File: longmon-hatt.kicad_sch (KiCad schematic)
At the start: 3 parts

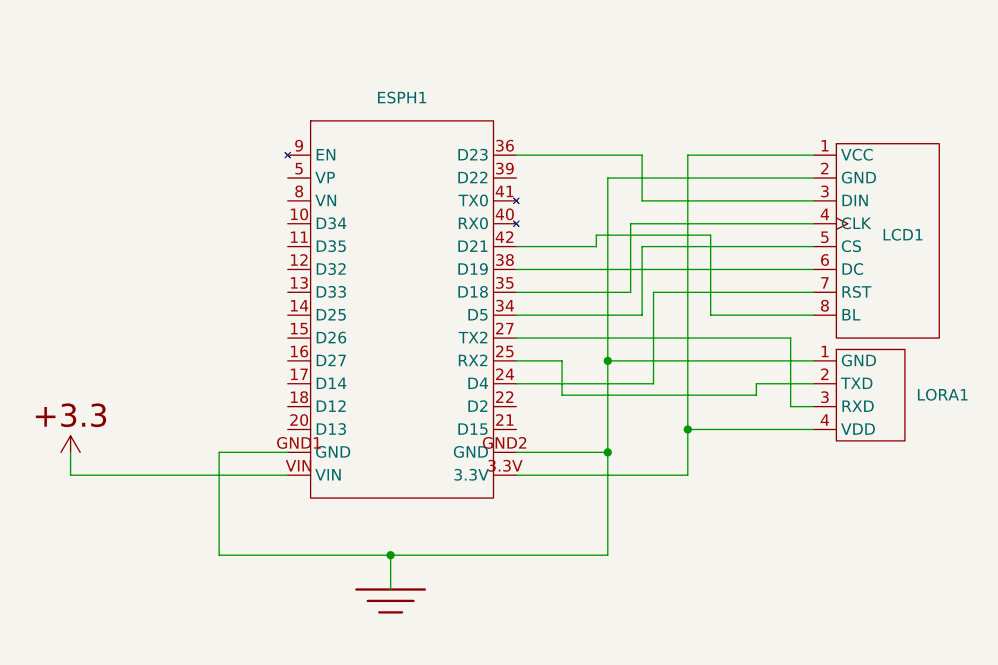
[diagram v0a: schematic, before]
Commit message: Modify LoRa module to include additional pin (unused)
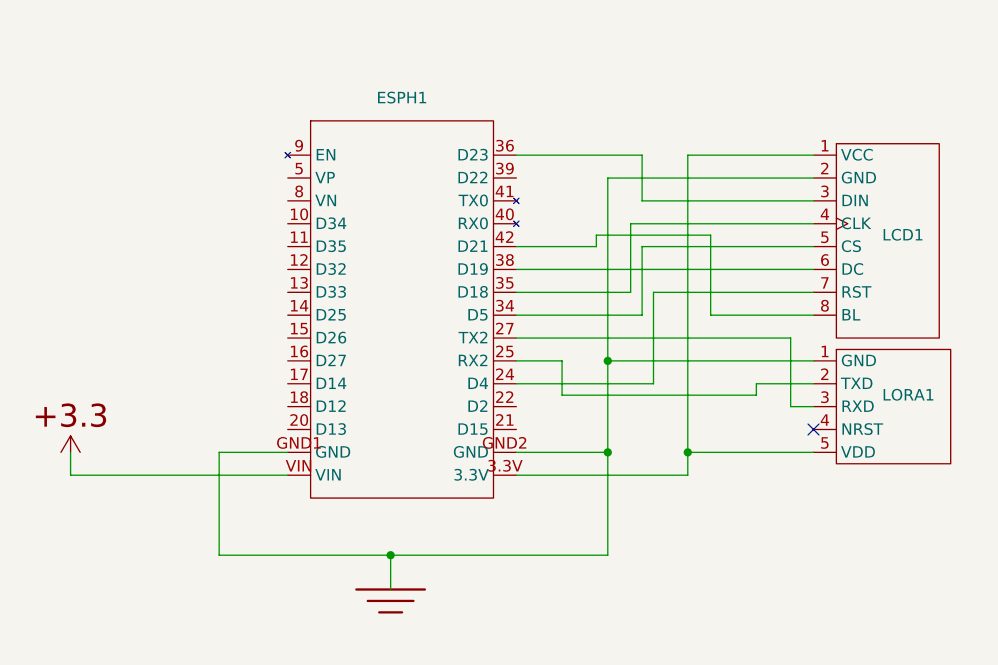
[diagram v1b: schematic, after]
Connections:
- net at ESPH1.3.3V, LCD1.1 (VCC): now also LORA1.5 (VDD); no longer LORA1.4 (VDD)
- no-connect marks 0 -> 1
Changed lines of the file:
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@@
 (kicad_sch (version 20230121) (generator eeschema)
   (paper "A4")
-  (junction (at 86.36 64.77) (diameter 0) (color 0 0 0 0)
+  (junction (at 86.36 67.31) (diameter 0) (color 0 0 0 0)
   )
   (junction (at 77.47 57.15) (diameter 0) (color 0 0 0 0)
@@
   (junction (at 53.34 78.74) (diameter 0) (color 0 0 0 0)
   )
+  (no_connect (at 100.33 64.77))
   (wire (pts (xy 17.78 69.85) (xy 41.91 69.85))
     (stroke (width 0) (type default))
@@
     (stroke (width 0) (type default))
   )
+  (wire (pts (xy 86.36 67.31) (xy 86.36 69.85))
+    (stroke (width 0) (type default))
+  )
   (wire (pts (xy 67.31 52.07) (xy 81.28 52.07))
     (stroke (width 0) (type default))
@@
     (stroke (width 0) (type default))
   )
-  (wire (pts (xy 86.36 64.77) (xy 86.36 69.85))
-    (stroke (width 0) (type default))
-  )
   (wire (pts (xy 100.33 36.83) (xy 77.47 36.83))
     (stroke (width 0) (type default))
@@
     (stroke (width 0) (type default))
   )
-  (wire (pts (xy 86.36 34.29) (xy 86.36 64.77))
+  (wire (pts (xy 86.36 34.29) (xy 86.36 67.31))
     (stroke (width 0) (type default))
   )
@@
     (stroke (width 0) (type default))
   )
-  (wire (pts (xy 86.36 64.77) (xy 100.33 64.77))
+  (wire (pts (xy 86.36 67.31) (xy 100.33 67.31))
     (stroke (width 0) (type default))
   )
@@
   (symbol (lib_id "ESP:LoRa_Module") (at 100.33 57.15 0) (unit 1)
     (in_bom yes) (on_board yes) (dnp no) (fields_autoplaced)
-    (property "Reference" "LORA1" (at 111.76 60.96 0)
+    (property "Reference" "LORA1" (at 107.95 60.96 0)
       (effects (font (size 1.27 1.27)) (justify left))
     )
@@
     (pin "3")
     (pin "4")
+    (pin "5")
     (instances
       (project "longmon-hatt"

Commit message: Close to final schematic, starting PCB I suck at PCB design
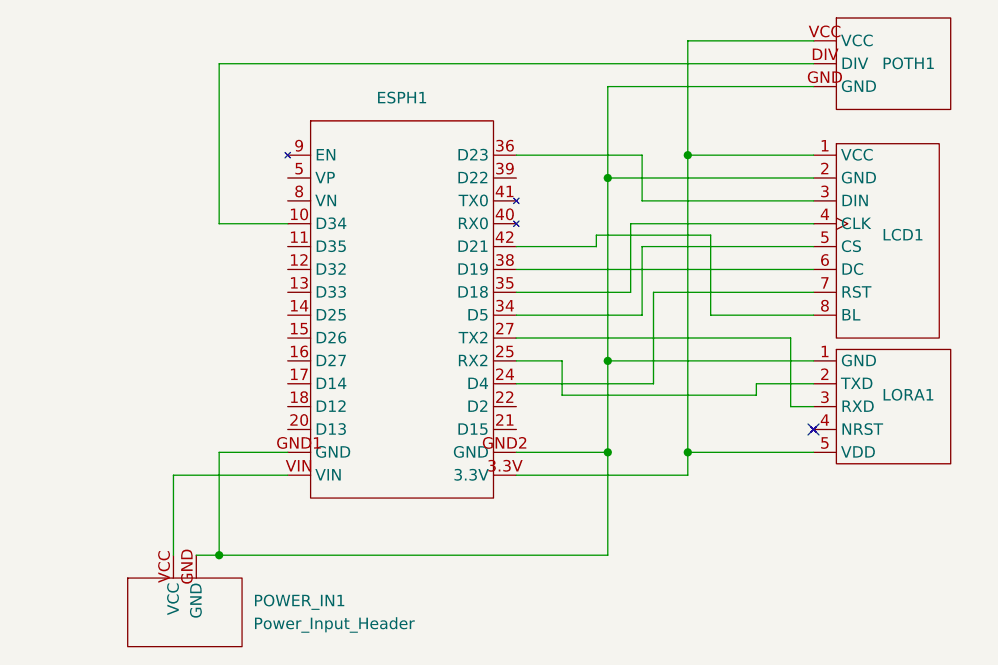
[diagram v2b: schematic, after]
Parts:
- added POTH1: ~, symbol ESP:Pot_Header
- added POWER_IN1: Power_Input_Header, symbol ESP:Power_Input_Header
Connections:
- net at ESPH1.10 (D34): now also POTH1.DIV
- net at ESPH1.3.3V, LCD1.1 (VCC), LORA1.5 (VDD): now also POTH1.VCC
- net +3.3: no longer names the net of ESPH1.VIN
- net +3.3: now also POWER_IN1.VCC
- net E: no longer names the net of ESPH1.GND1 (GND), ESPH1.GND2 (GND), LCD1.2 (GND), LORA1.1 (GND)
- net E: now also POTH1.GND, POWER_IN1.GND
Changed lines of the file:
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@@
   (junction (at 86.36 67.31) (diameter 0) (color 0 0 0 0)
   )
+  (junction (at 34.29 78.74) (diameter 0) (color 0 0 0 0)
+  )
   (junction (at 77.47 57.15) (diameter 0) (color 0 0 0 0)
   )
+  (junction (at 86.36 34.29) (diameter 0) (color 0 0 0 0)
+  )
+  (junction (at 77.47 36.83) (diameter 0) (color 0 0 0 0)
+  )
   (junction (at 77.47 67.31) (diameter 0) (color 0 0 0 0)
   )
-  (junction (at 53.34 78.74) (diameter 0) (color 0 0 0 0)
-  )
   (no_connect (at 100.33 64.77))
-  (wire (pts (xy 17.78 69.85) (xy 41.91 69.85))
+  (wire (pts (xy 77.47 26.67) (xy 77.47 36.83))
     (stroke (width 0) (type default))
   )
@@
     (stroke (width 0) (type default))
   )
+  (wire (pts (xy 34.29 24.13) (xy 34.29 41.91))
+    (stroke (width 0) (type default))
+  )
   (wire (pts (xy 81.28 34.29) (xy 81.28 39.37))
     (stroke (width 0) (type default))
@@
     (stroke (width 0) (type default))
   )
+  (wire (pts (xy 34.29 41.91) (xy 41.91 41.91))
+    (stroke (width 0) (type default))
+  )
   (wire (pts (xy 100.33 59.69) (xy 93.98 59.69))
     (stroke (width 0) (type default))
@@
     (stroke (width 0) (type default))
   )
+  (wire (pts (xy 100.33 24.13) (xy 34.29 24.13))
+    (stroke (width 0) (type default))
+  )
   (wire (pts (xy 72.39 57.15) (xy 67.31 57.15))
     (stroke (width 0) (type default))
@@
     (stroke (width 0) (type default))
   )
-  (wire (pts (xy 17.78 67.31) (xy 17.78 69.85))
-    (stroke (width 0) (type default))
-  )
   (wire (pts (xy 81.28 52.07) (xy 81.28 44.45))
     (stroke (width 0) (type default))
@@
     (stroke (width 0) (type default))
   )
-  (wire (pts (xy 53.34 78.74) (xy 34.29 78.74))
-    (stroke (width 0) (type default))
-  )
   (wire (pts (xy 82.55 49.53) (xy 100.33 49.53))
     (stroke (width 0) (type default))
@@
     (stroke (width 0) (type default))
   )
+  (wire (pts (xy 86.36 21.59) (xy 100.33 21.59))
+    (stroke (width 0) (type default))
+  )
   (wire (pts (xy 97.79 54.61) (xy 97.79 62.23))
     (stroke (width 0) (type default))
@@
     (stroke (width 0) (type default))
   )
-  (wire (pts (xy 77.47 78.74) (xy 53.34 78.74))
+  (wire (pts (xy 31.75 78.74) (xy 34.29 78.74))
+    (stroke (width 0) (type default))
+  )
+  (wire (pts (xy 86.36 34.29) (xy 86.36 21.59))
+    (stroke (width 0) (type default))
+  )
+  (wire (pts (xy 34.29 78.74) (xy 77.47 78.74))
+    (stroke (width 0) (type default))
+  )
+  (wire (pts (xy 29.21 69.85) (xy 41.91 69.85))
     (stroke (width 0) (type default))
   )
@@
     (stroke (width 0) (type default))
   )
+  (wire (pts (xy 29.21 69.85) (xy 29.21 78.74))
+    (stroke (width 0) (type default))
+  )
   (wire (pts (xy 77.47 57.15) (xy 77.47 67.31))
     (stroke (width 0) (type default))
@@
     (stroke (width 0) (type default))
   )
+  (wire (pts (xy 100.33 26.67) (xy 77.47 26.67))
+    (stroke (width 0) (type default))
+  )
   (wire (pts (xy 77.47 36.83) (xy 77.47 57.15))
     (stroke (width 0) (type default))
@@
     (stroke (width 0) (type default))
   )
-  (wire (pts (xy 53.34 78.74) (xy 53.34 82.55))
-    (stroke (width 0) (type default))
-  )
   (wire (pts (xy 67.31 59.69) (xy 82.55 59.69))
     (stroke (width 0) (type default))
@@
   (wire (pts (xy 81.28 39.37) (xy 100.33 39.37))
     (stroke (width 0) (type default))
-  )
-  (symbol (lib_id "PCM_Generic:P,E") (at 53.34 82.55 0) (unit 1)
-    (in_bom yes) (on_board yes) (dnp no) (fields_autoplaced)
-    (property "Reference" "#PWR01" (at 57.15 78.74 0)
-      (effects (font (size 2.54 2.54)) (justify left) hide)
-    )
-    (property "Value" "P,E" (at 57.15 82.55 0)
-      (effects (font (size 0 0)) (justify left) hide)
-    )
-    (property "Footprint" "" (at 53.34 82.55 0)
-      (effects (font (size 2.54 2.54)) hide)
-    )
-    (property "Datasheet" "" (at 53.34 82.55 0)
-      (effects (font (size 2.54 2.54)) hide)
-    )
-    (pin "0")
-    (instances
-      (project "longmon-hatt"
-        (path "/fc493522-7015-405f-abaf-84a4f5d09cfd"
-          (reference "#PWR01") (unit 1)
-        )
-      )
-    )
   )
   (symbol (lib_id "ESP:ESP_Devkit_Header") (at 54.61 52.07 0) (unit 1)
@@
     (pin "2")
     (pin "3")
+    (pin "5")
     (pin "4")
-    (pin "5")
     (instances
       (project "longmon-hatt"
@@
     )
   )
-  (symbol (lib_id "PCM_Generic:P,+3.3") (at 17.78 67.31 0) (unit 1)
+  (symbol (lib_id "ESP:Power_Input_Header") (at 29.21 78.74 0) (unit 1)
     (in_bom yes) (on_board yes) (dnp no) (fields_autoplaced)
-    (property "Reference" "#PWR02" (at 20.32 67.31 0)
-      (effects (font (size 2.54 2.54)) (justify left) hide)
-    )
-    (property "Value" "P,+3.3" (at 17.78 64.77 0)
-      (effects (font (size 0 0)) (justify bottom) hide)
-    )
-    (property "Footprint" "" (at 17.78 67.31 0)
-      (effects (font (size 2.54 2.54)) hide)
-    )
-    (property "Datasheet" "" (at 17.78 67.31 0)
-      (effects (font (size 2.54 2.54)) hide)
-    )
-    (pin "0")
-    (instances
-      (project "longmon-hatt"
-        (path "/fc493522-7015-405f-abaf-84a4f5d09cfd"
-          (reference "#PWR02") (unit 1)
-        )
-      )
+    (property "Reference" "POWER_IN1" (at 38.1 83.82 0)
+      (effects (font (size 1.27 1.27)) (justify left))
+    )
+    (property "Value" "Power_Input_Header" (at 38.1 86.36 0)
+      (effects (font (size 1.27 1.27)) (justify left))
+    )
+    (property "Footprint" "" (at 29.21 78.74 0)
+      (effects (font (size 1.27 1.27)) hide)
+    )
+    (property "Datasheet" "" (at 29.21 78.74 0)
+      (effects (font (size 1.27 1.27)) hide)
+    )
+    (pin "GND")
+    (pin "VCC")
+    (instances
+      (project "longmon-hatt"
+        (path "/fc493522-7015-405f-abaf-84a4f5d09cfd"
+          (reference "POWER_IN1") (unit 1)
+        )
+      )
+    )
+  )
+  (symbol (lib_id "ESP:Pot_Header") (at 100.33 21.59 0) (unit 1)
+    (in_bom yes) (on_board yes) (dnp no)
+    (property "Reference" "POTH1" (at 107.95 24.13 0)
+      (effects (font (size 1.27 1.27)) (justify left))
+    )
+    (property "Value" "~" (at 100.33 21.59 0)
+      (effects (font (size 1.27 1.27)))
+    )
+    (property "Footprint" "" (at 100.33 21.59 0)
+      (effects (font (size 1.27 1.27)) hide)
+    )
+    (property "Datasheet" "" (at 100.33 21.59 0)
+      (effects (font (size 1.27 1.27)) hide)
+    )
+    (pin "DIV")
+    (pin "GND")
+    (pin "VCC")
+    (instances
+      (project "longmon-hatt"
+        (path "/fc493522-7015-405f-abaf-84a4f5d09cfd"
+          (reference "POTH1") (unit 1)
+        )
+      )

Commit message: Add LoRa header (TODO: fix pin order), add edge cut
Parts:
- LORA1: footprint (none) -> ESP:LoRa Header
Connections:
- no-connect marks 1 -> 0
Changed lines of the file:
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@@
   (junction (at 77.47 67.31) (diameter 0) (color 0 0 0 0)
   )
-  (no_connect (at 100.33 64.77))
   (wire (pts (xy 77.47 26.67) (xy 77.47 36.83))
     (stroke (width 0) (type default))
@@
       (effects (font (size 1.27 1.27)))
     )
-    (property "Footprint" "" (at 100.33 57.15 0)
-      (effects (font (size 1.27 1.27)) hide)
-    )
+    (property "Footprint" "ESP:LoRa Header" (at 100.33 57.15 0)
+      (effects (font (size 1.27 1.27)) hide)
+    )

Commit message: Fix LoRa pins and pads, add design constraints
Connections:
- net at ESPH1.25 (RX2): now also LORA1.3 (TXD); no longer LORA1.2 (TXD)
- net at ESPH1.27 (TX2): now also LORA1.4 (RXD); no longer LORA1.3 (RXD)
- net at ESPH1.3.3V, LCD1.1 (VCC), POTH1.VCC: now also LORA1.6 (VDD); no longer LORA1.5 (VDD)
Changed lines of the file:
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@@
     )
     (pin "1")
-    (pin "2")
     (pin "3")
+    (pin "4")
+    (pin "6")
     (pin "5")
-    (pin "4")
     (instances
       (project "longmon-hatt"

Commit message: Add POT header
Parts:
- removed POWER_IN1: Power_Input_Header, symbol ESP:Power_Input_Header
- POTH1: footprint (none) -> ESP:POT Header
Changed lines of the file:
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@@
   (junction (at 86.36 67.31) (diameter 0) (color 0 0 0 0)
   )
-  (junction (at 34.29 78.74) (diameter 0) (color 0 0 0 0)
-  )
   (junction (at 77.47 57.15) (diameter 0) (color 0 0 0 0)
   )
@@
     (stroke (width 0) (type default))
   )
-  (wire (pts (xy 31.75 78.74) (xy 34.29 78.74))
-    (stroke (width 0) (type default))
-  )
   (wire (pts (xy 86.36 34.29) (xy 86.36 21.59))
     (stroke (width 0) (type default))
@@
     (stroke (width 0) (type default))
   )
-  (wire (pts (xy 29.21 69.85) (xy 41.91 69.85))
-    (stroke (width 0) (type default))
-  )
   (wire (pts (xy 67.31 44.45) (xy 76.2 44.45))
-    (stroke (width 0) (type default))
-  )
-  (wire (pts (xy 29.21 69.85) (xy 29.21 78.74))
     (stroke (width 0) (type default))
   )
@@
     )
   )
-  (symbol (lib_id "ESP:Power_Input_Header") (at 29.21 78.74 0) (unit 1)
-    (in_bom yes) (on_board yes) (dnp no) (fields_autoplaced)
-    (property "Reference" "POWER_IN1" (at 38.1 83.82 0)
-      (effects (font (size 1.27 1.27)) (justify left))
-    )
-    (property "Value" "Power_Input_Header" (at 38.1 86.36 0)
-      (effects (font (size 1.27 1.27)) (justify left))
-    )
-    (property "Footprint" "" (at 29.21 78.74 0)
-      (effects (font (size 1.27 1.27)) hide)
-    )
-    (property "Datasheet" "" (at 29.21 78.74 0)
-      (effects (font (size 1.27 1.27)) hide)
-    )
-    (pin "GND")
-    (pin "VCC")
-    (instances
-      (project "longmon-hatt"
-        (path "/fc493522-7015-405f-abaf-84a4f5d09cfd"
-          (reference "POWER_IN1") (unit 1)
-        )
-      )
-    )
-  )
   (symbol (lib_id "ESP:Pot_Header") (at 100.33 21.59 0) (unit 1)
     (in_bom yes) (on_board yes) (dnp no)
@@
       (effects (font (size 1.27 1.27)))
     )
-    (property "Footprint" "" (at 100.33 21.59 0)
+    (property "Footprint" "ESP:POT Header" (at 100.33 21.59 0)
       (effects (font (size 1.27 1.27)) hide)
     )
@@
       (effects (font (size 1.27 1.27)) hide)
     )
+    (property "Sim.Enable" "0" (at 100.33 21.59 0)
+      (effects (font (size 1.27 1.27)) hide)
+    )
